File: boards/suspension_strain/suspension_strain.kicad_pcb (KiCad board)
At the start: 2 copper layers, 70 x 70 mm, 84 parts, among them IC1 ATMEGA16M1, J1 micromatch_female_RA_18, J2 micromatch_female_RA_12, P1 CONN_02X03, U1 TPS561201, U2 CAN_Transceiver, U3 MCP6001RT, U4 MCP6001RT, U5 MCP6001RT, U6 MCP6001RT, U7 MCP6001RT, U8 MCP6001RT, Y1 Crystal_SMD

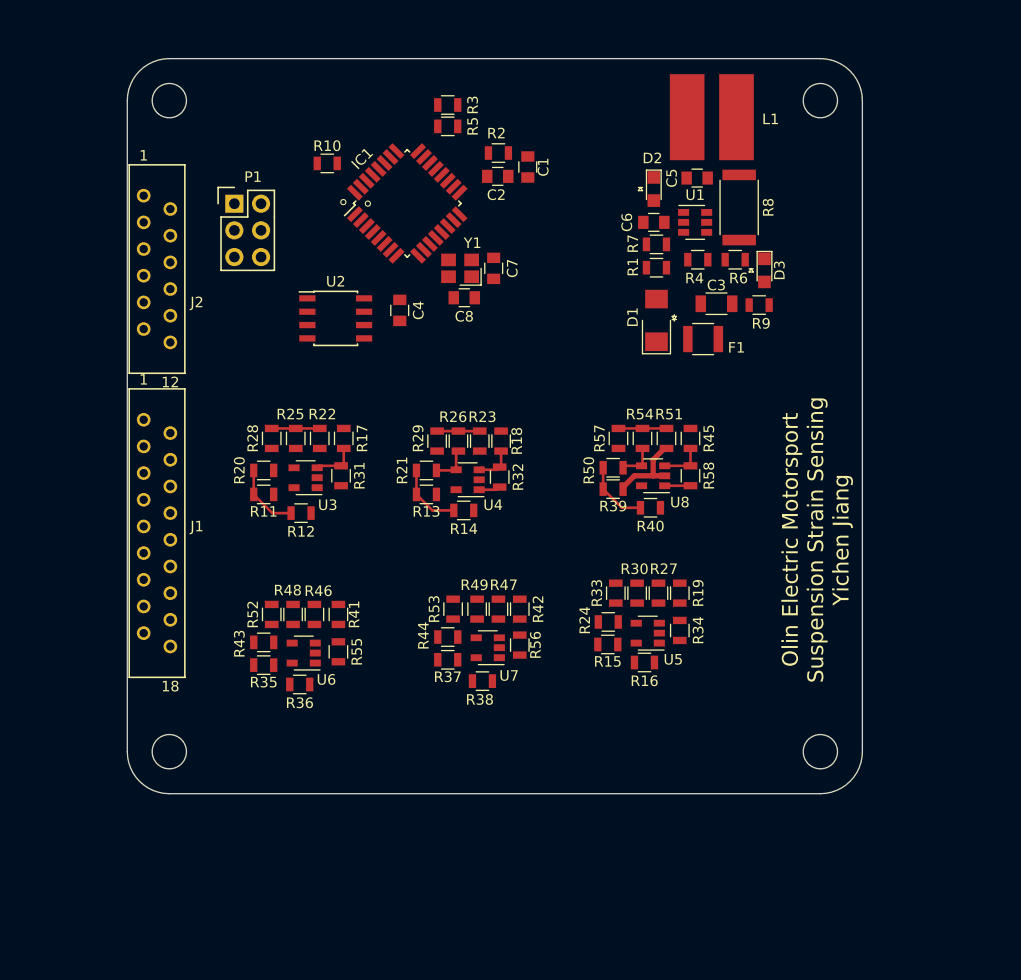
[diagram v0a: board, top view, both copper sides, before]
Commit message: finish tracing for suspension strain sensing board
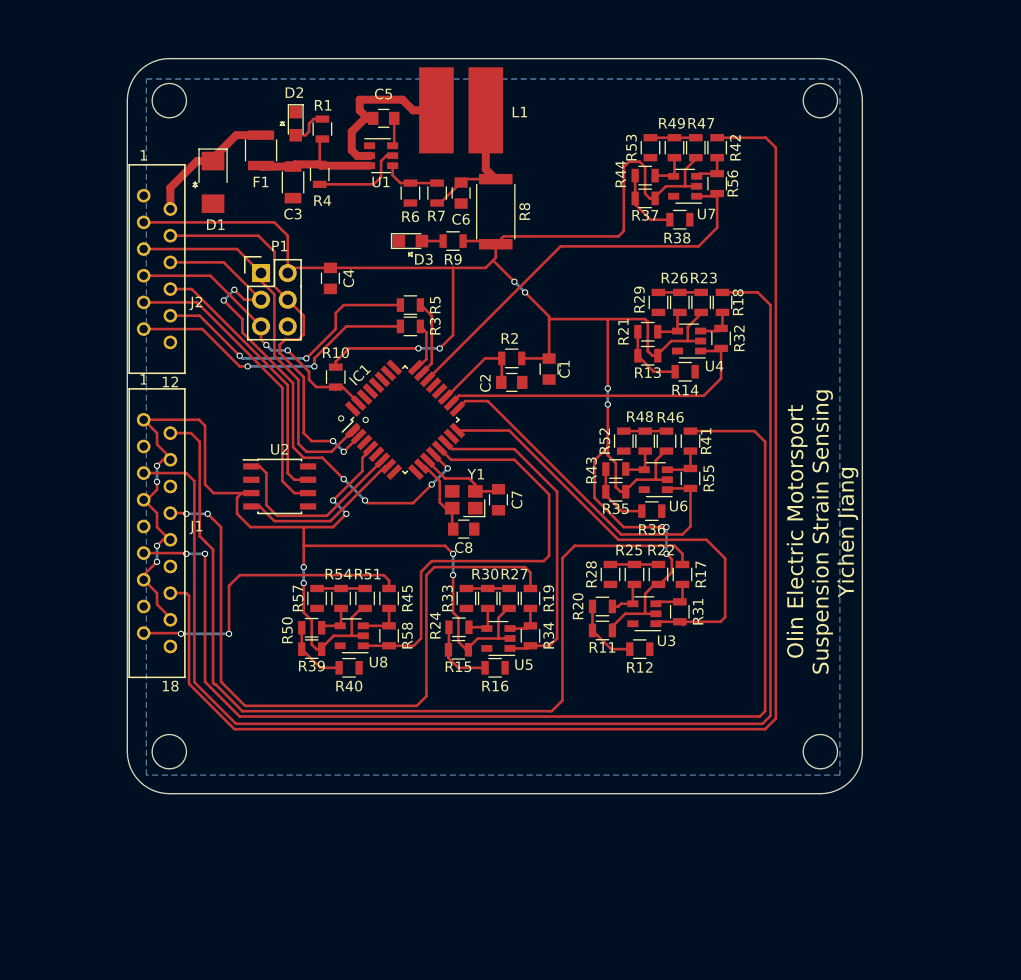
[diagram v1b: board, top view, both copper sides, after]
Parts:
- moved R38 47.8 mm to (166.1, 85.3)
- moved R37 47.8 mm to (162.8, 83.3)
- moved R44 47.8 mm to (162.8, 81.1)
- moved R56 47.8 mm to (169.7, 81.9)
- moved R42 47.8 mm to (169.7, 78.5)
- moved R47 47.8 mm to (167.6, 78.5)
- moved R49 47.8 mm to (165.6, 78.5)
- moved R53 47.8 mm to (163.3, 78.5)
- moved U7 47.8 mm to (166.6, 82.2)
- moved F1 45.8 mm to (126.2, 78.7), turned to 270 degrees
- moved D1 44.2 mm to (121.7, 81.8), turned to 270 degrees
- moved C3 41.9 mm to (129.3, 81.8), turned to 270 degrees
- moved R36 37.4 mm to (163.4, 113.1)
- moved R35 37.4 mm to (160.0, 111.3)
- moved R43 37.4 mm to (160.0, 109.1)
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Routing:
- net VCC: track 9.60 -> 304.1 mm, vias 0 -> 18
- net /Gauge5_MID: track 0.00 -> 128.7 mm
- net /Gauge2_MID: track 0.00 -> 125.3 mm
- net /Gauge4_MID: track 0.00 -> 106.2 mm, vias 0 -> 2
- net /Gauge1_MID: track 0.00 -> 88.2 mm
- net /Gauge3_MID: track 0.00 -> 64.5 mm, vias 0 -> 2
- net /SCK: track 0.00 -> 52.2 mm, vias 0 -> 6
- net Net-(IC1-Pad16): track 0.26 -> 43.7 mm
- net Net-(IC1-Pad13): track 2.46 -> 43.1 mm
- net Net-(IC1-Pad22): track 0.00 -> 39.2 mm
- net /MISO: track 0.00 -> 39.0 mm
- net /MOSI: track 0.00 -> 38.7 mm, vias 0 -> 2
- net Net-(IC1-Pad17): track 0.00 -> 34.0 mm
- net Net-(IC1-Pad14): track 0.00 -> 31.5 mm
- net Net-(IC1-Pad18): track 2.41 -> 32.3 mm
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- added copper zone on B.Cu, net GND
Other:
- net class Default: trace_width 0.1524 -> 2.54
- rule trace_min: 0.1524 -> 0.254

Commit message: updated schemetic and layout
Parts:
- added D4: LED_0805, footprints:LED_0805_OEM, F.Cu at (135.9, 115.1)
- added D5: LED_0805, footprints:LED_0805_OEM, F.Cu at (140.1, 115.1)
- added R59: R_200, footprints:R_0805_OEM, F.Cu at (138.4, 112.0)
- added R60: R_200, footprints:R_0805_OEM, F.Cu at (141.4, 112.6)
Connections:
- IC1 pad 8: Net-(IC1-Pad8) -> /P_LED_1
- IC1 pad 9: Net-(IC1-Pad9) -> /P_LED_2
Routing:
- net GND: track 0.00 -> 240.2 mm, vias 0 -> 21
- net VCC: track 304.1 -> 377.5 mm, vias 18 -> 2
- net /Gauge2_MID: track 125.3 -> 119.0 mm
- net /Gauge5_MID: track 128.7 -> 122.5 mm
- net /Gauge4_MID: track 106.2 -> 100.1 mm
- net Net-(D4-Pad2): track 0.00 -> 4.29 mm
- net /SCK: track 52.2 -> 48.5 mm, vias 6 -> 4
- net /P_LED_1: track 0.00 -> 2.76 mm
- net /P_LED_2: track 0.00 -> 2.41 mm
- net Net-(D5-Pad2): track 0.00 -> 1.66 mm
- net /Gauge3_MID: track 64.5 -> 62.9 mm, vias 2 -> 4
- net /MISO: track 39.0 -> 38.0 mm
- net Net-(J2-Pad10): track 26.6 -> 25.8 mm
- net Net-(R20-Pad1): track 4.54 -> 3.74 mm
- net Net-(R50-Pad1): track 4.30 -> 3.53 mm
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- added copper zone on F.Cu, net VCC
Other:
- net class Default: via_dia 0.6 -> 0.6096; via_drill 0.4 -> 0.3048
- rule via_min_drill: 0.3 -> 0.3048
- rule via_min_size: 0.4 -> 0.6096

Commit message: final check
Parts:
- moved R18 0.57 mm to (170.8, 93.2)
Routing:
- net VCC: track 377.5 -> 398.7 mm
- net GND: track 240.2 -> 219.5 mm, vias 21 -> 22
- net /Gauge2_MID: track 119.0 -> 118.5 mm
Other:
- board text added: "12V Power"
- board text added: "5V Power"
- board text added: "No.1"
- board text added: "No.2"
- board text added: "No.3"
- board text added: "No.4"
- board text added: "No.5"
- board text added: "No.6"
- board text added: "Olin Electric Motorsport Suspension Strain Sensing v.1 Yichen Jiang"
- board text added: "PB2"
- board text added: "PC4"
- board text added: "PC5"
- board text added: "PC6"
- board text added: "PD5"
- board text added: "PD6"
- board text added: "P_LED"
- board text removed: "Olin Electric Motorsport Suspension Strain Sensing Yichen Jiang"
